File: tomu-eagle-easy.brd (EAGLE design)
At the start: 24.8 x 10.2 mm, 18 parts, among them U1 EFM32HG309F64G

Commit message: more fixes
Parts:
- moved - 1.05 mm to (10.8, 1.78)
- moved C 0.57 mm to (13.7, 1.78)
- moved D 0.57 mm to (16.3, 1.78)
- moved LED2 0.25 mm to (21.1, 2.03)
- moved R1 0.25 mm to (21.1, 3.05)
- moved 5V 0.25 mm to (9.14, 1.78)
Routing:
- net +3V3: track 3.23 -> 26.6 mm, vias 0 -> 5
- net CAP1B: track 0.00 -> 9.71 mm, vias 0 -> 2
- net CAP0B: track 0.00 -> 7.67 mm, vias 0 -> 2
- net CAP1A: track 0.00 -> 7.25 mm, vias 0 -> 1
- net CAP0A: track 0.00 -> 5.20 mm, vias 0 -> 1
- net USB_D+: track 9.32 -> 10.6 mm
- net N$5: track 0.00 -> 1.13 mm
- net N$4: track 0.00 -> 1.06 mm
- net DBG_SWDIO: track 3.01 -> 2.25 mm
- net GND: track 13.9 -> 14.5 mm, vias 3 -> 4
- net VUSB: track 15.9 -> 15.4 mm

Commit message: small updates to tomu-eagle-easy
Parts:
- C2, C3: device adafruit:C0402K -> adafruit:C0402
- moved C 0.26 mm to (13.7, 1.52)
- moved D 0.25 mm to (16.3, 1.52)
- moved 5V 0.10 mm to (9.24, 1.75)
- moved C3 0.10 mm to (11.4, 6.70)
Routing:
- net VUSB: track 15.4 -> 20.2 mm
- net USB_D+: track 10.6 -> 8.60 mm
- net CAP0A: track 5.20 -> 6.05 mm, vias 1 -> 2
- net CAP1B: track 9.71 -> 10.3 mm, vias 2 -> 3
- net CAP1A: track 7.25 -> 7.70 mm, vias 1 -> 2
- net CAP0B: track 7.67 -> 7.53 mm, vias 2 -> 3
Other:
- board text added: "tomu-eagle-easy"

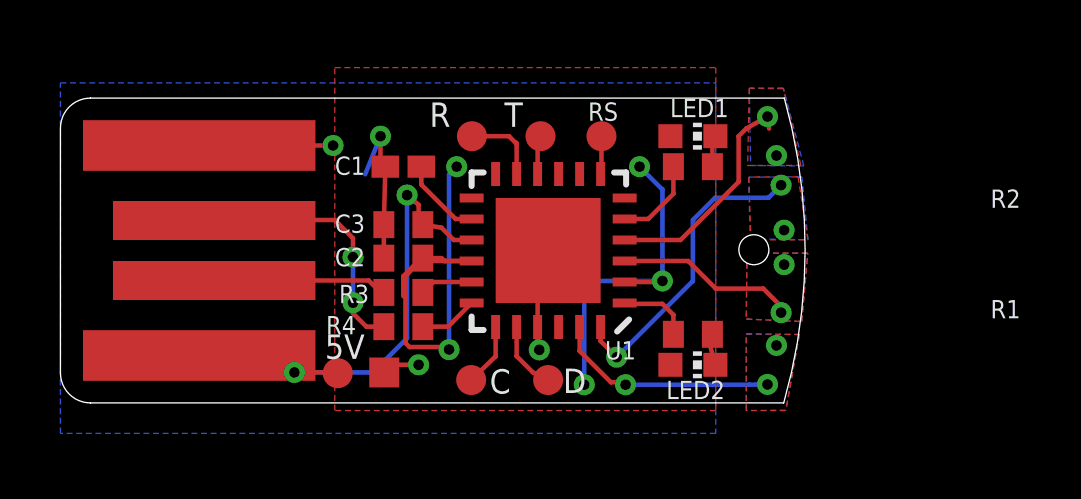
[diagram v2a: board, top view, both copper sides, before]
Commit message: added tomo-pro-micro breakout board
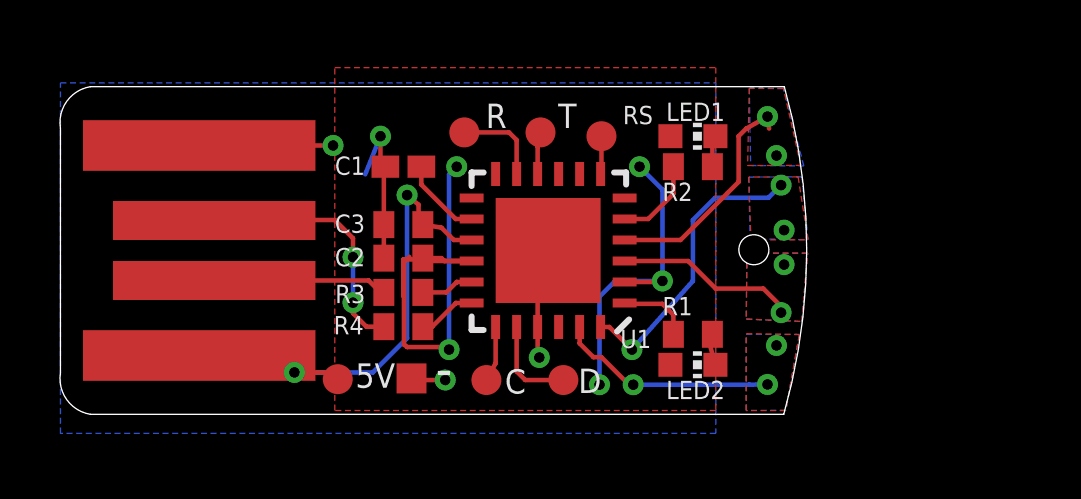
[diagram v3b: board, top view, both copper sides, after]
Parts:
- moved - 0.93 mm to (11.7, 1.58)
- moved C 0.51 mm to (14.2, 1.52)
- moved D 0.51 mm to (16.8, 1.52)
- moved R 0.28 mm to (13.5, 9.78)
- moved 5V 0.20 mm to (9.24, 1.55)
- moved T 0.13 mm to (16.0, 9.78)
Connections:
- net RUSB_D+ renamed RUSB_P
- net RUSB_D- renamed RUSB_N
- net USB_D+ renamed USB_P
- net USB_D- renamed USB_N
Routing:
- net DBG_SWDIO: track 2.31 -> 3.16 mm
- net GND: track 14.8 -> 15.4 mm
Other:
- board size 24.8 x 10.2 mm -> 24.9 x 10.9 mm

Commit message: LED resistors should be 75 not 15 (or maybe 52 as in the tomu bom)
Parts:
- R1, R2: value 15 -> 75
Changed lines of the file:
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@@
 <?xml version="1.0" encoding="utf-8"?>
 <!DOCTYPE eagle SYSTEM "eagle.dtd">
-<eagle version="8.6.3">
+<eagle version="8.7.1">
 <drawing>
 <settings>
@@
 <attribute name="VALUE" x="20.447" y="0.127" size="1.27" layer="27"/>
 </element>
-<element name="R1" library="adafruit" library_urn="urn:adsk.eagle:library:420" package="R0402" value="15" x="21.082" y="3.048" smashed="yes" rot="R180">
+<element name="R1" library="adafruit" library_urn="urn:adsk.eagle:library:420" package="R0402" value="75" x="21.082" y="3.048" smashed="yes" rot="R180">
 <attribute name="NAME" x="20.066" y="3.683" size="0.6096" layer="25" ratio="12"/>
 <attribute name="VALUE" x="21.717" y="5.08" size="1.27" layer="27" rot="R180"/>
 </element>
-<element name="R2" library="adafruit" library_urn="urn:adsk.eagle:library:420" package="R0402" value="15" x="21.082" y="8.636" smashed="yes" rot="R180">
+<element name="R2" library="adafruit" library_urn="urn:adsk.eagle:library:420" package="R0402" value="75" x="21.082" y="8.636" smashed="yes" rot="R180">
 <attribute name="NAME" x="20.066" y="7.493" size="0.6096" layer="25" ratio="12"/>
 <attribute name="VALUE" x="21.717" y="10.668" size="1.27" layer="27" rot="R180"/>
